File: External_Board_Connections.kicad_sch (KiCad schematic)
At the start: 14 parts, among them J1 Conn_01x04, J10 Conn_01x02, J11 Conn_01x06, J12 Conn_01x02, J14 Conn_01x02, J19 Conn_01x01_Socket, J2 Conn_01x04, J20 Conn_01x01_Socket, J21 Conn_01x01_Socket, J22 Conn_01x01_Socket, J6 Conn_02x04_Odd_Even, J7 Conn_02x04_Odd_Even, J8 Conn_02x04_Odd_Even, J9 Conn_02x04_Odd_Even

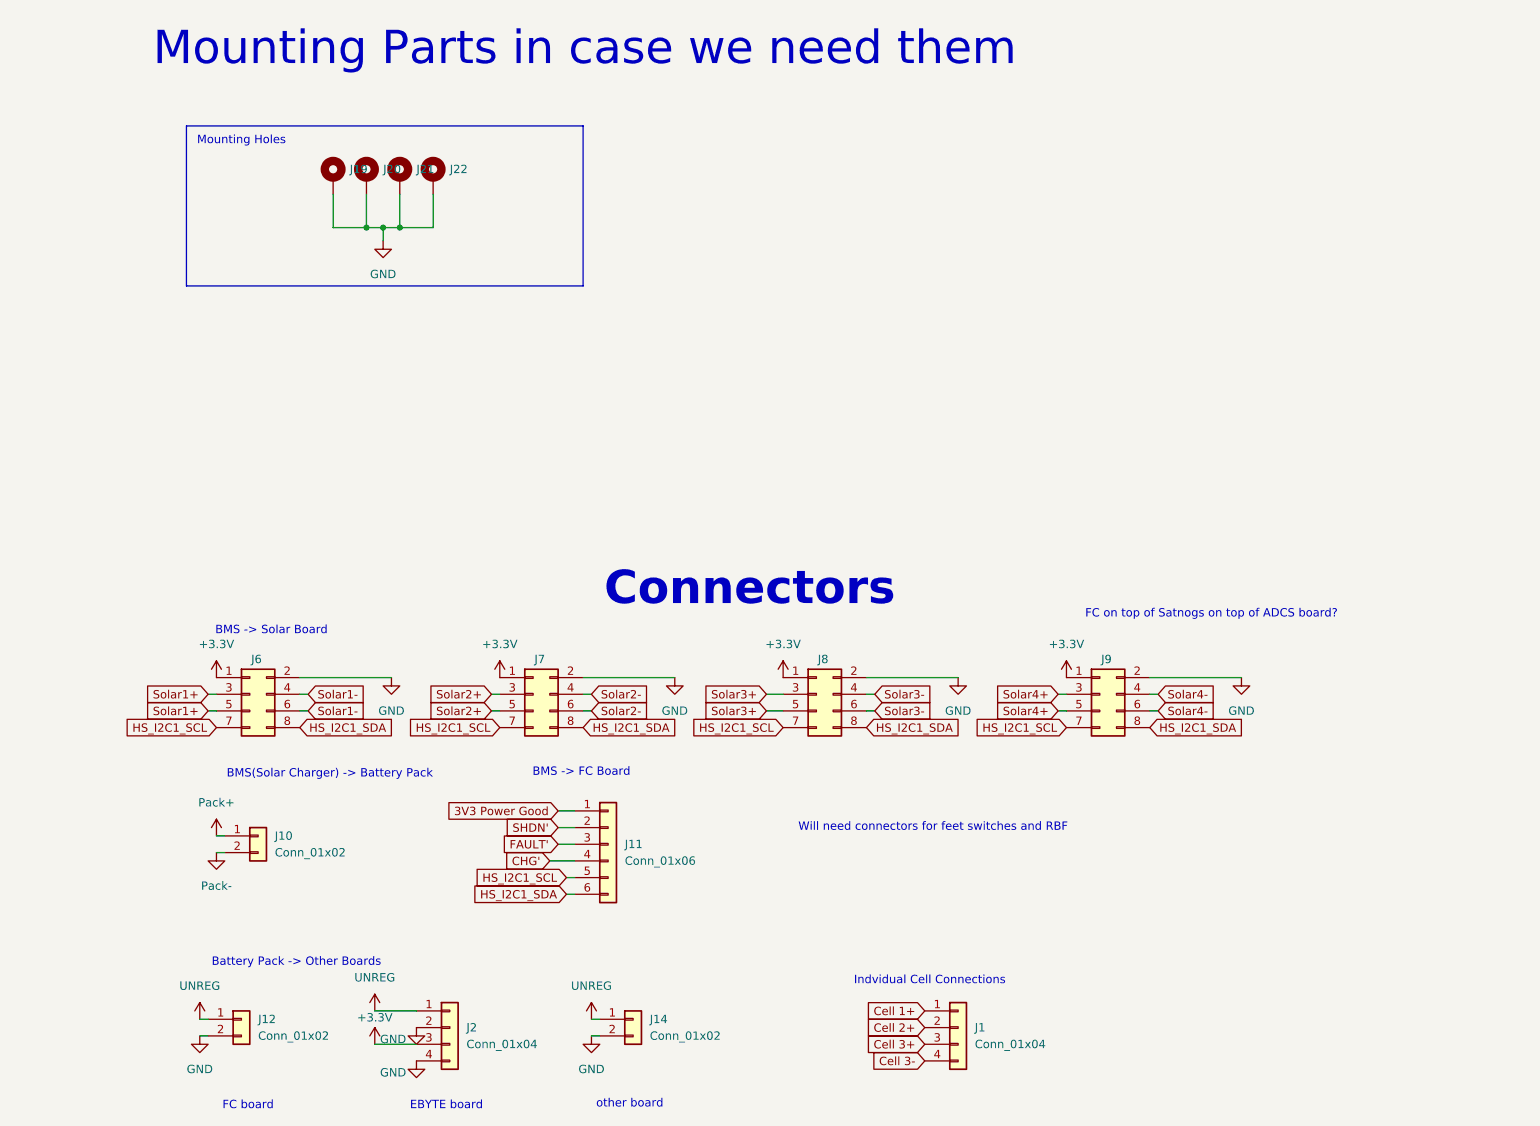
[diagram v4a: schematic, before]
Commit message: Footprint fixes and cleaning up
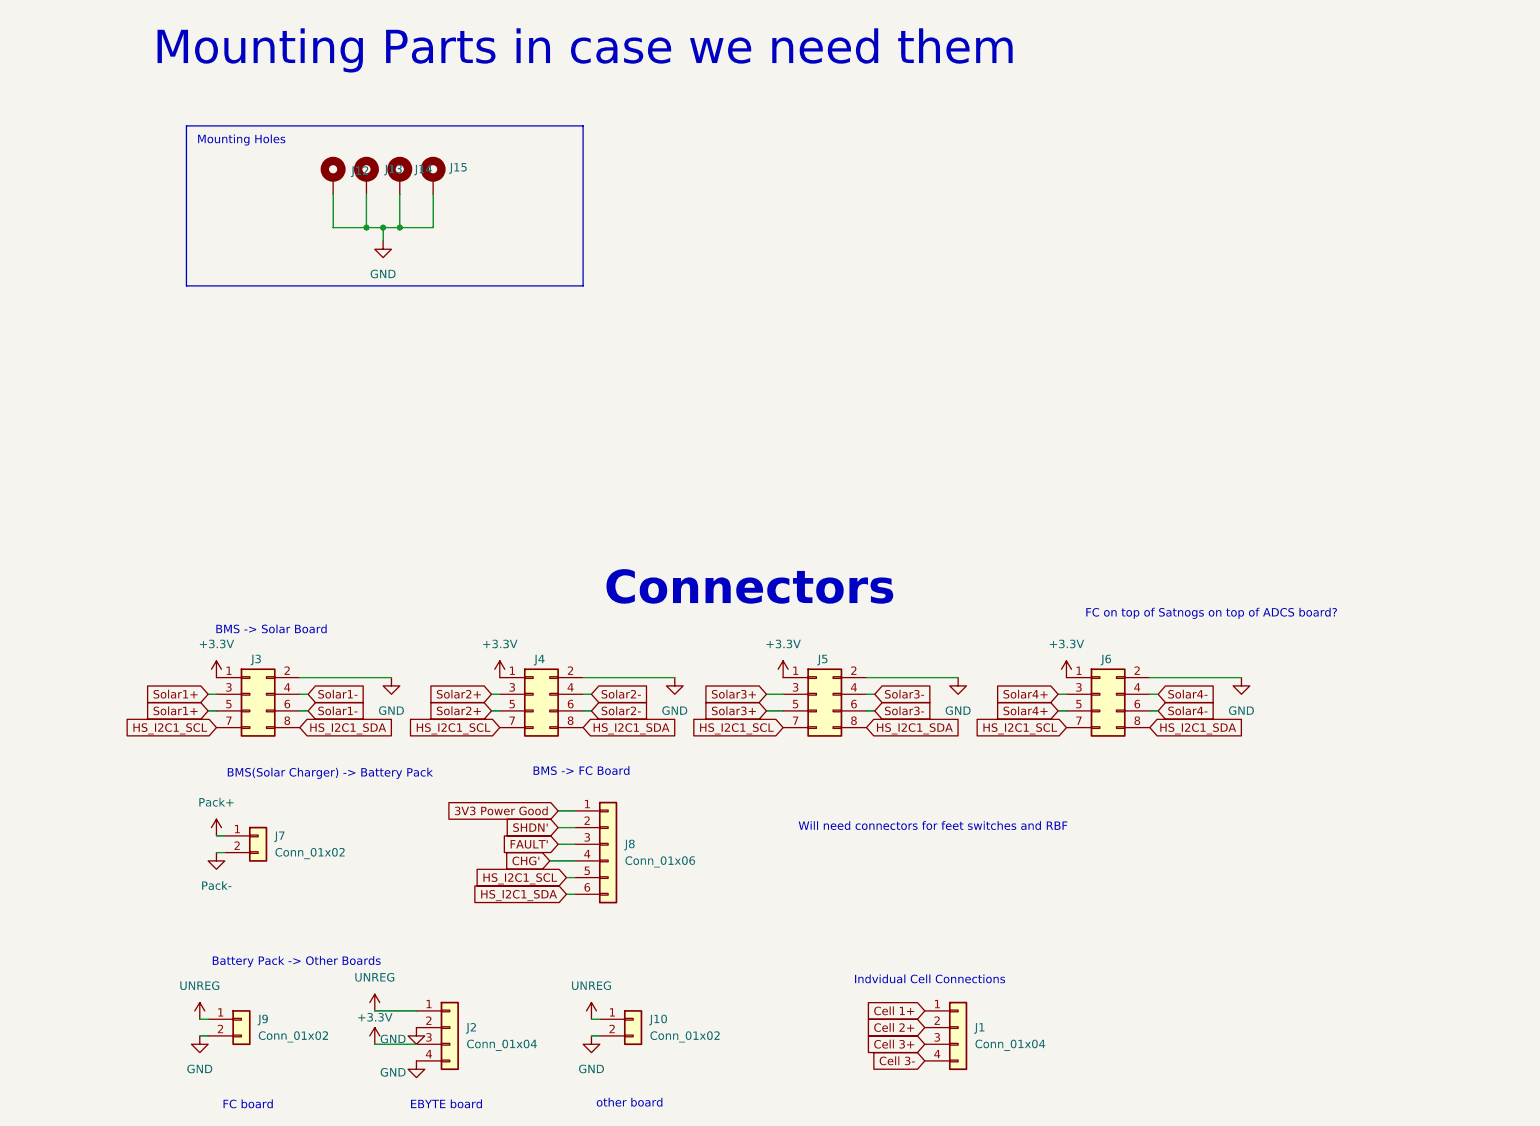
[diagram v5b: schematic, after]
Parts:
- renumbered J14 to J10, J19 to J12, J20 to J13, J21 to J14, J22 to J15, J6 to J3, J7 to J4, J8 to J5, J9 to J6, J10 to J7, J11 to J8, J12 to J9
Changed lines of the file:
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@@
 		(dnp no)
 		(fields_autoplaced yes)
-		(property "Reference" "J14"
+		(property "Reference" "J10"
 			(at 101.6 167.6399 0)
 			(show_name no)
@@
 			(project "BMS_Board_Prototype"
 				(path "/4ee99911-836b-4752-8a2d-327c8b28dc47/420608bc-a1a4-412d-a20e-6570cff27a90"
-					(reference "J14")
+					(reference "J10")
 					(unit 1)
 				)
@@
 		(in_pos_files yes)
 		(dnp no)
-		(property "Reference" "J7"
+		(property "Reference" "J4"
 			(at 84.836 112.776 0)
 			(show_name no)
@@
 			(project "BMS_Board_Prototype"
 				(path "/4ee99911-836b-4752-8a2d-327c8b28dc47/420608bc-a1a4-412d-a20e-6570cff27a90"
-					(reference "J7")
+					(reference "J4")
 					(unit 1)
 				)
@@
 		(dnp no)
 		(fields_autoplaced yes)
-		(property "Reference" "J12"
+		(property "Reference" "J9"
 			(at 41.91 167.6399 0)
 			(show_name no)
@@
 			(project "BMS_Board_Prototype"
 				(path "/4ee99911-836b-4752-8a2d-327c8b28dc47/420608bc-a1a4-412d-a20e-6570cff27a90"
-					(reference "J12")
+					(reference "J9")
 					(unit 1)
 				)
@@
 		(in_pos_files yes)
 		(dnp no)
-		(fields_autoplaced yes)
-		(property "Reference" "J20"
-			(at 60.96 38.0999 0)
+		(property "Reference" "J13"
+			(at 61.214 38.1 0)
 			(show_name no)
 			(do_not_autoplace no)
@@
 			(project "BMS_Board_Prototype"
 				(path "/4ee99911-836b-4752-8a2d-327c8b28dc47/420608bc-a1a4-412d-a20e-6570cff27a90"
-					(reference "J20")
+					(reference "J13")
 					(unit 1)
 				)
@@
 		(in_pos_files yes)
 		(dnp no)
-		(property "Reference" "J9"
+		(property "Reference" "J6"
 			(at 171.196 112.776 0)
 			(show_name no)
@@
 			(project "BMS_Board_Prototype"
 				(path "/4ee99911-836b-4752-8a2d-327c8b28dc47/420608bc-a1a4-412d-a20e-6570cff27a90"
-					(reference "J9")
+					(reference "J6")
 					(unit 1)
 				)
@@
 		(in_pos_files yes)
 		(dnp no)
-		(fields_autoplaced yes)
-		(property "Reference" "J19"
-			(at 55.88 38.0999 0)
+		(property "Reference" "J12"
+			(at 56.134 38.354 0)
 			(show_name no)
 			(do_not_autoplace no)
@@
 			(project "BMS_Board_Prototype"
 				(path "/4ee99911-836b-4752-8a2d-327c8b28dc47/420608bc-a1a4-412d-a20e-6570cff27a90"
-					(reference "J19")
+					(reference "J12")
 					(unit 1)
 				)
@@
 		(in_pos_files yes)
 		(dnp no)
-		(property "Reference" "J6"
+		(property "Reference" "J3"
 			(at 41.656 112.776 0)
 			(show_name no)
@@
 			(project "BMS_Board_Prototype"
 				(path "/4ee99911-836b-4752-8a2d-327c8b28dc47/420608bc-a1a4-412d-a20e-6570cff27a90"
-					(reference "J6")
+					(reference "J3")
 					(unit 1)
 				)
@@
 		(in_pos_files yes)
 		(dnp no)
-		(fields_autoplaced yes)
-		(property "Reference" "J21"
-			(at 66.04 38.0999 0)
+		(property "Reference" "J14"
+			(at 65.786 38.1 0)
 			(show_name no)
 			(do_not_autoplace no)
@@
 			(project "BMS_Board_Prototype"
 				(path "/4ee99911-836b-4752-8a2d-327c8b28dc47/420608bc-a1a4-412d-a20e-6570cff27a90"
-					(reference "J21")
+					(reference "J14")
 					(unit 1)
 				)
@@
 		(dnp no)
 		(fields_autoplaced yes)
-		(property "Reference" "J10"
+		(property "Reference" "J7"
 			(at 44.45 139.6999 0)
 			(show_name no)
@@
 			(project "BMS_Board_Prototype"
 				(path "/4ee99911-836b-4752-8a2d-327c8b28dc47/420608bc-a1a4-412d-a20e-6570cff27a90"
-					(reference "J10")
+					(reference "J7")
 					(unit 1)
 				)
@@
 		(in_pos_files yes)
 		(dnp no)
-		(property "Reference" "J8"
+		(property "Reference" "J5"
 			(at 128.016 112.776 0)
 			(show_name no)
@@
 			(project "BMS_Board_Prototype"
 				(path "/4ee99911-836b-4752-8a2d-327c8b28dc47/420608bc-a1a4-412d-a20e-6570cff27a90"
-					(reference "J8")
+					(reference "J5")
 					(unit 1)
 				)
@@
 		(in_pos_files yes)
 		(dnp no)
-		(fields_autoplaced yes)
-		(property "Reference" "J22"
-			(at 71.12 38.0999 0)
+		(property "Reference" "J15"
+			(at 71.12 37.846 0)
 			(show_name no)
 			(do_not_autoplace no)
@@
 			(project "BMS_Board_Prototype"
 				(path "/4ee99911-836b-4752-8a2d-327c8b28dc47/420608bc-a1a4-412d-a20e-6570cff27a90"
-					(reference "J22")
+					(reference "J15")
 					(unit 1)
 				)
@@
 		(dnp no)
 		(fields_autoplaced yes)
-		(property "Reference" "J11"
+		(property "Reference" "J8"
 			(at 97.79 140.9699 0)
 			(show_name no)
@@
 			(project "BMS_Board_Prototype"
 				(path "/4ee99911-836b-4752-8a2d-327c8b28dc47/420608bc-a1a4-412d-a20e-6570cff27a90"
-					(reference "J11")
-					(unit 1)
-				)
+					(reference "J8")
+					(unit 1)
+				)

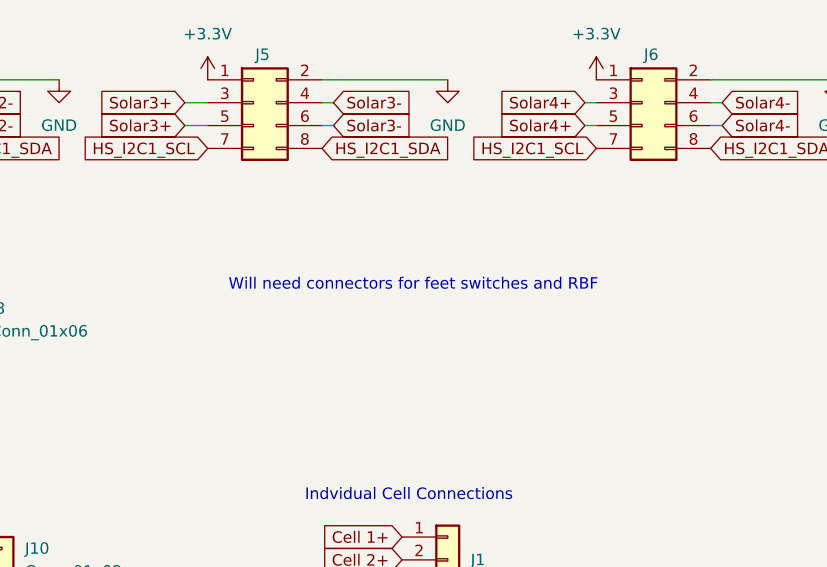
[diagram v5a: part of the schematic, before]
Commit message: Updates for bat manager and OV/OC protection
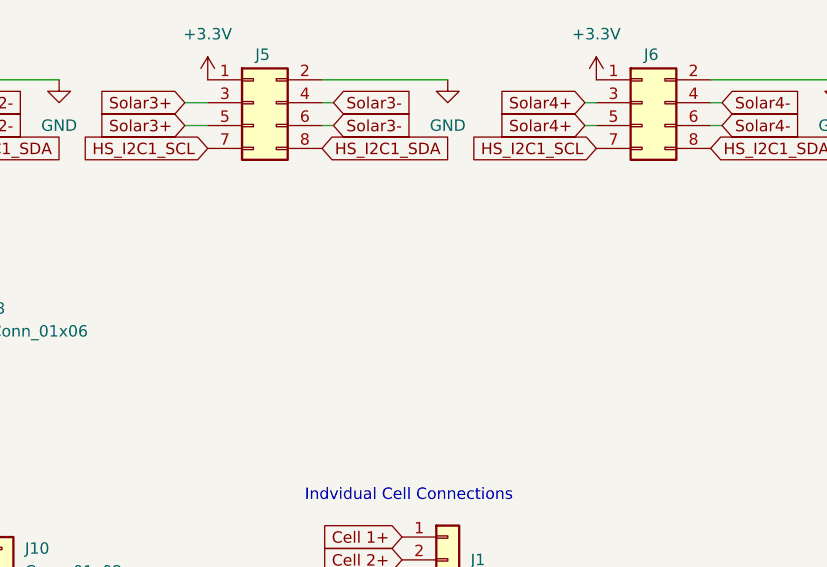
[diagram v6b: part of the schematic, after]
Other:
- note removed: "Will need connectors for feet switches and RBF"
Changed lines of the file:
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@@
-		)
-	)
-	(text "Will need connectors for feet switches and RBF"
-		(exclude_from_sim no)
-		(at 144.78 138.43 0)
-		(effects
-			(font
-				(size 1.27 1.27)
-			)
 		)
 	)

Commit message: Adding in Test points
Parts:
- added TP10: S3+, symbol Connector:TestPoint
- added TP11: S3-, symbol Connector:TestPoint
- added TP12: S4+, symbol Connector:TestPoint
- added TP13: S4-, symbol Connector:TestPoint
- added TP6: S1+, symbol Connector:TestPoint
- added TP7: S1-, symbol Connector:TestPoint
- added TP8: S2+, symbol Connector:TestPoint
- added TP9: S2-, symbol Connector:TestPoint
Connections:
- net Pack+ is gone; now on net Cell 1+: J7.1 (Pin_1)
- net Pack- is gone; now on net Cell 3-: J7.2 (Pin_2)
- net Solar1+: now also TP6.1
- net Solar1-: now also TP7.1
- net Solar2+: now also TP8.1
- net Solar2-: now also TP9.1
- net Solar3+: now also TP10.1
- net Solar3-: now also TP11.1
- net Solar4+: now also TP12.1
- net Solar4-: now also TP13.1
- net GND renamed VSS

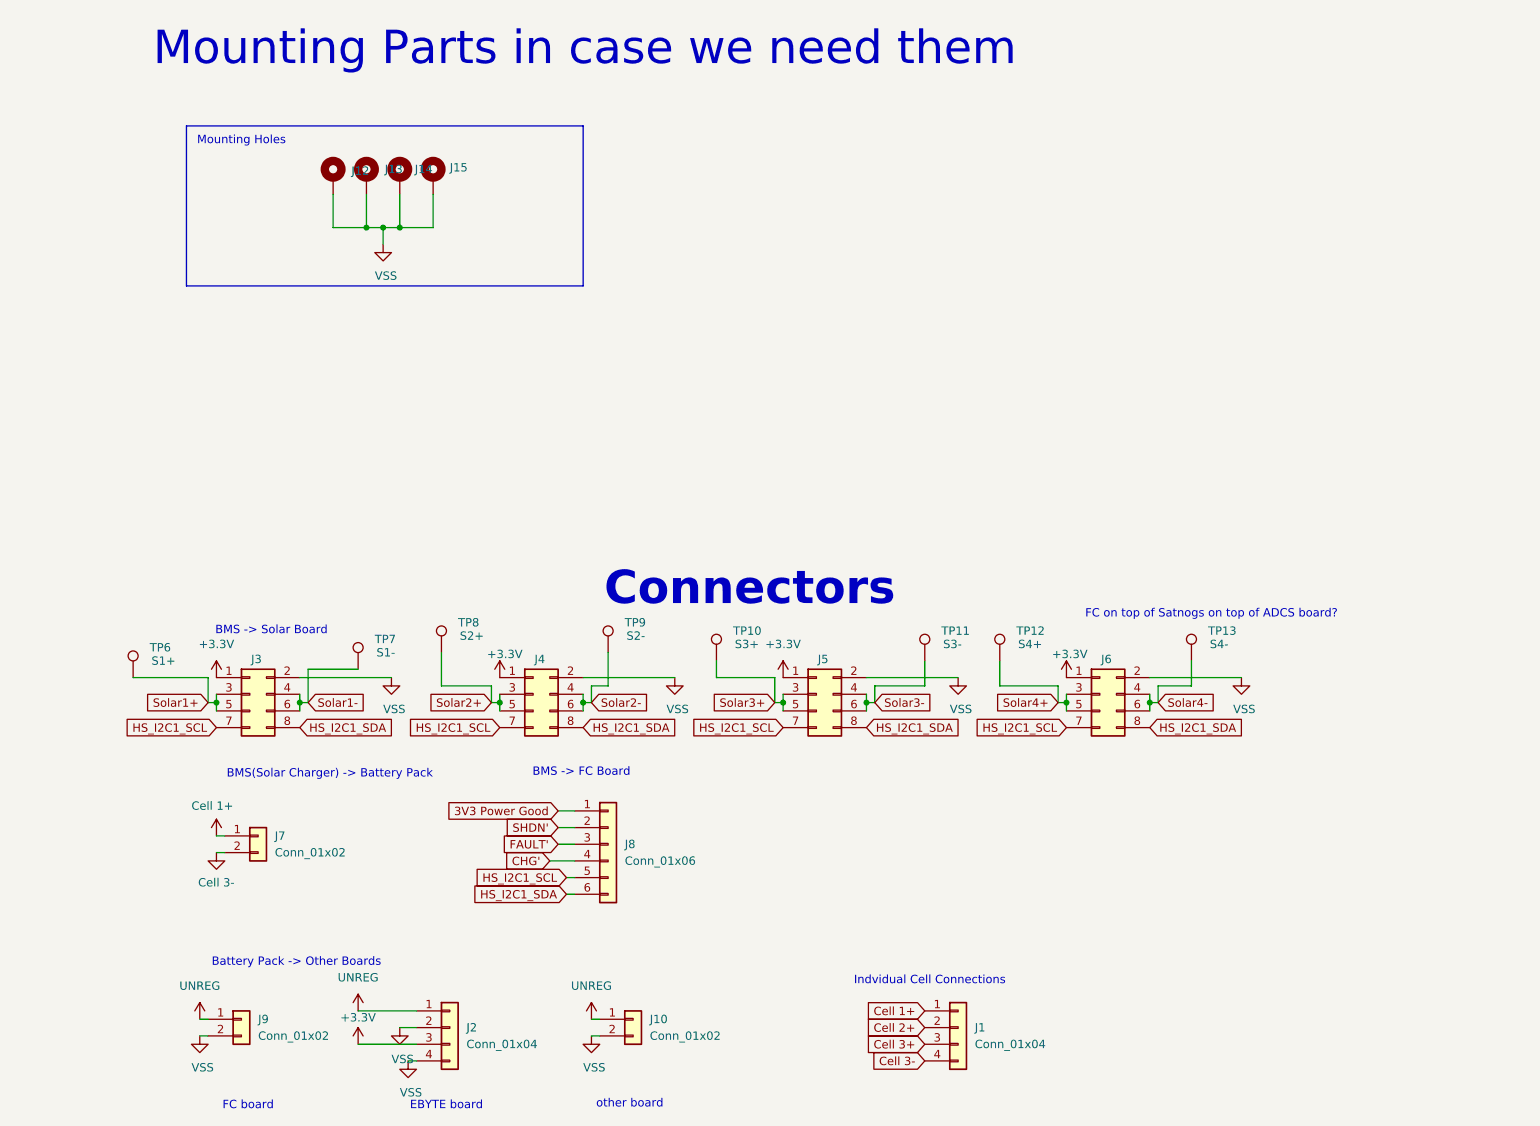
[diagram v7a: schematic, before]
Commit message: Updates for debug and RBF
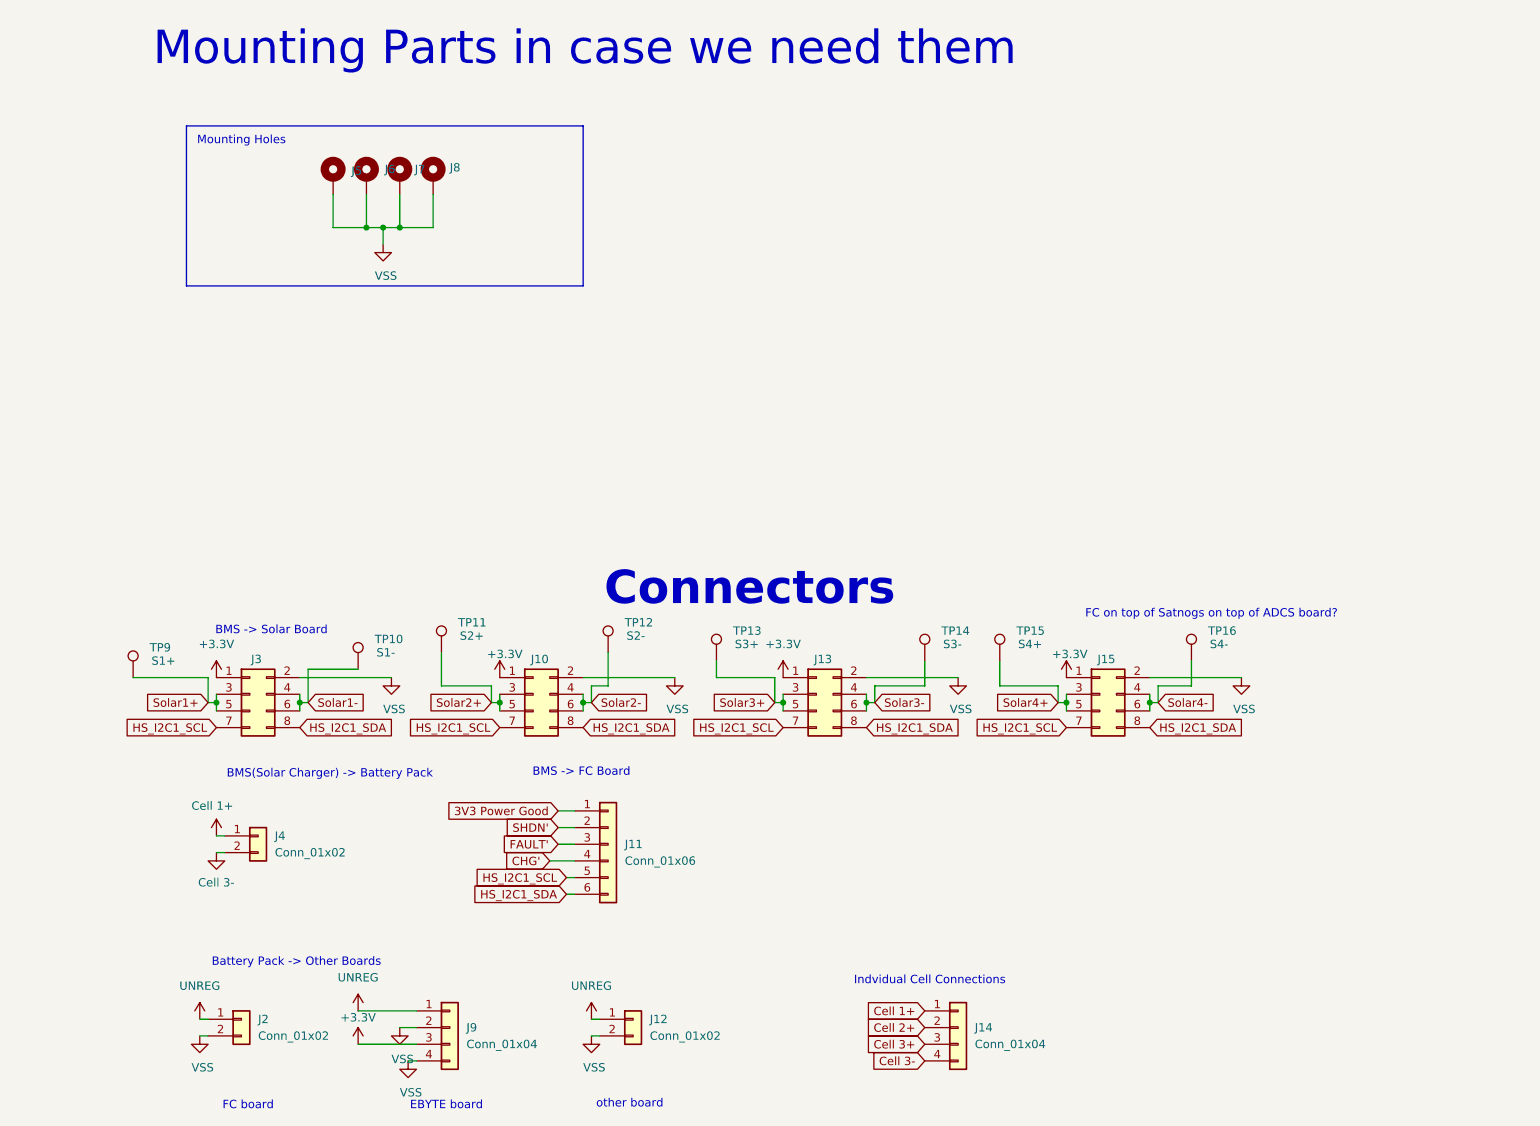
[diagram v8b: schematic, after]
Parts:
- renumbered J4 to J10, J8 to J11, J10 to J12, J5 to J13, J1 to J14, J6 to J15, J9 to J2, J7 to J4, J12 to J5, J13 to J6, J14 to J7, J15 to J8, J2 to J9, TP7 to TP10, TP8 to TP11, TP9 to TP12, TP10 to TP13, TP11 to TP14, TP12 to TP15, TP13 to TP16, TP6 to TP9
